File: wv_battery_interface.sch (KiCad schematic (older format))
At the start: 5 parts, among them J1 Conn_01x03, J11 Conn_01x03, J2 Conn_01x03, J3 Conn_01x04, U1 ATtiny204-SS

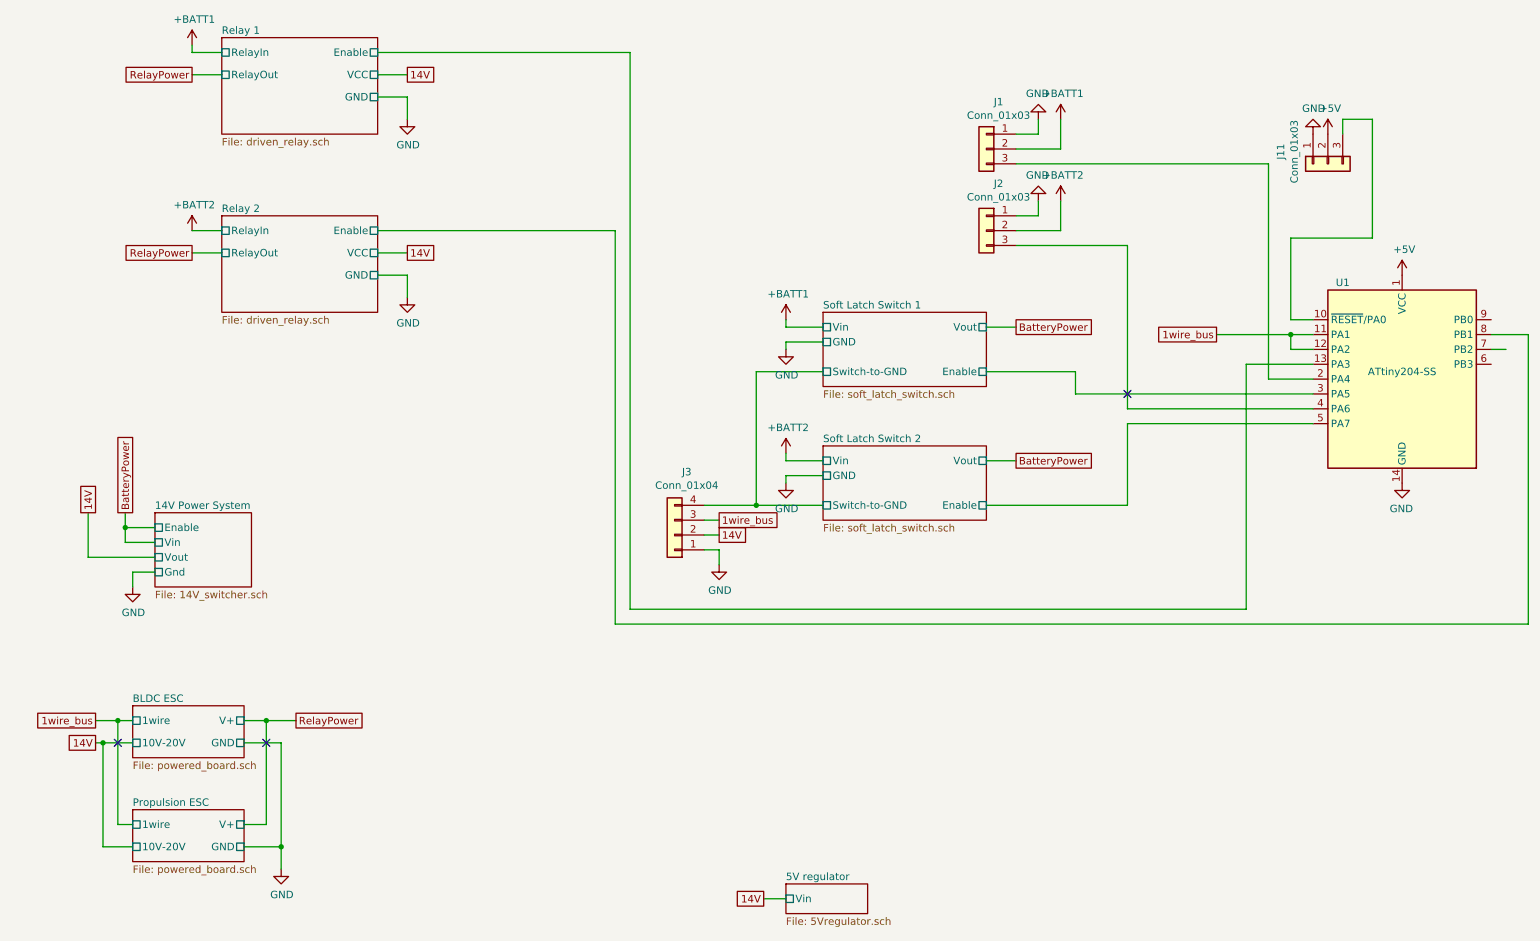
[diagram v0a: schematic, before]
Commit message: schematic update
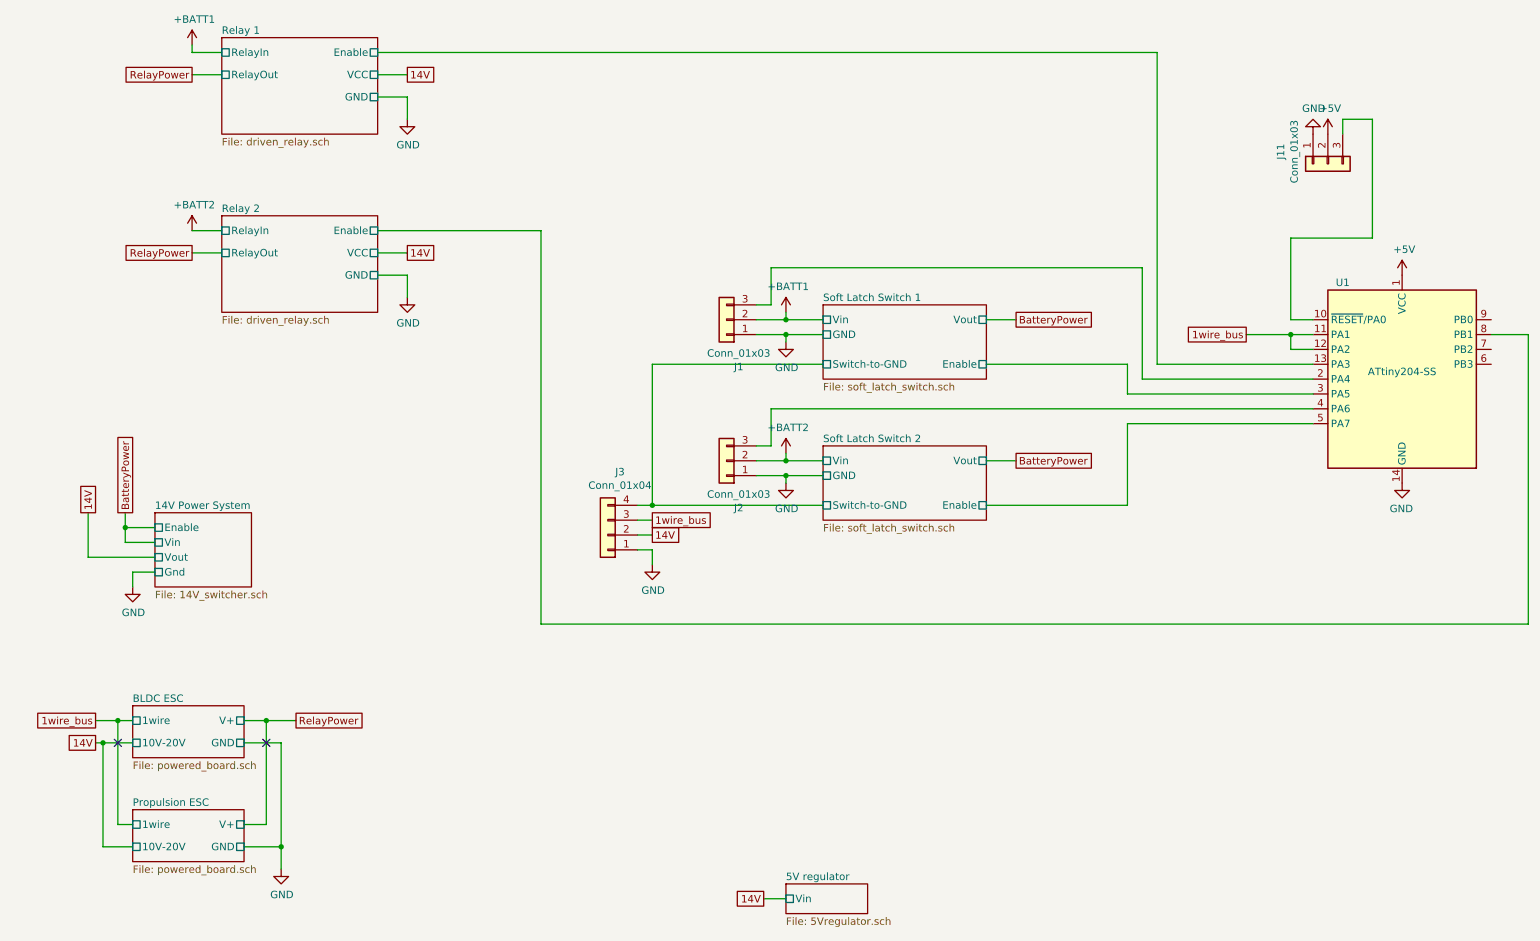
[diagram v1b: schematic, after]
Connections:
- no-connect marks 3 -> 2
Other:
- moved on the sheet: J1, J2, J3
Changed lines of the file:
@@
 $EndDescr
-$Comp
-L Connector_Generic:Conn_01x03 J1
-U 1 1 616238A4
-P 7250 2000
-F 0 "J1" H 7168 2317 50  0000 C CNN
-F 1 "Conn_01x03" H 7168 2226 50  0000 C CNN
-F 2 "Connector_Wire:SolderWire-2sqmm_1x03_P7.8mm_D2mm_OD3.9mm" H 7250 2000 50  0001 C CNN
-F 3 "~" H 7250 2000 50  0001 C CNN
-	1    7250 2000
-	-1   0    0    -1
-$EndComp
-$Comp
-L Connector_Generic:Conn_01x03 J2
-U 1 1 61623D8A
-P 7250 2550
-F 0 "J2" H 7168 2867 50  0000 C CNN
-F 1 "Conn_01x03" H 7168 2776 50  0000 C CNN
-F 2 "Connector_Wire:SolderWire-2sqmm_1x03_P7.8mm_D2mm_OD3.9mm" H 7250 2550 50  0001 C CNN
-F 3 "~" H 7250 2550 50  0001 C CNN
-	1    7250 2550
-	-1   0    0    -1
-$EndComp
-Wire Wire Line
-	7600 1900 7600 1800
-Wire Wire Line
-	7750 2000 7750 1800
-Wire Wire Line
-	7450 2450 7600 2450
-Wire Wire Line
-	7600 2450 7600 2350
-Wire Wire Line
-	7450 2550 7750 2550
-Wire Wire Line
-	7750 2550 7750 2350
-$Comp
-L power_symbols:+BATT1 #PWR0101
-U 1 1 61636C34
-P 7750 1800
-F 0 "#PWR0101" H 7750 1650 50  0001 C CNN
-F 1 "+BATT1" H 7765 1973 50  0000 C CNN
-F 2 "" H 7750 1800 50  0001 C CNN
-F 3 "" H 7750 1800 50  0001 C CNN
-	1    7750 1800
-	1    0    0    -1
-$EndComp
-Wire Wire Line
-	7450 2000 7750 2000
-Wire Wire Line
-	7450 1900 7600 1900
 $Comp
 L power_symbols:+BATT1 #PWR0106
@@
 L power_symbols:+BATT1 #PWR0107
 U 1 1 6168E4A3
-P 5900 3150
-F 0 "#PWR0107" H 5900 3000 50  0001 C CNN
-F 1 "+BATT1" H 5915 3323 50  0000 C CNN
-F 2 "" H 5900 3150 50  0001 C CNN
-F 3 "" H 5900 3150 50  0001 C CNN
-	1    5900 3150
-	1    0    0    -1
-$EndComp
-$Comp
-L power_symbols:+BATT2 #PWR0103
-U 1 1 61637B76
-P 7750 2350
-F 0 "#PWR0103" H 7750 2200 50  0001 C CNN
-F 1 "+BATT2" H 7765 2523 50  0000 C CNN
-F 2 "" H 7750 2350 50  0001 C CNN
-F 3 "" H 7750 2350 50  0001 C CNN
-	1    7750 2350
+P 5900 3100
+F 0 "#PWR0107" H 5900 2950 50  0001 C CNN
+F 1 "+BATT1" H 5915 3273 50  0000 C CNN
+F 2 "" H 5900 3100 50  0001 C CNN
+F 3 "" H 5900 3100 50  0001 C CNN
+	1    5900 3100
 	1    0    0    -1
 $EndComp
@@
 	1    0    0    -1
 $EndComp
-$Sheet
-S 6150 3100 1100 500
-U 6173FDB3
-F0 "Soft Latch Switch 1" 50
-F1 "soft_latch_switch.sch" 50
-F2 "Vin" U L 6150 3200 50
-F3 "GND" U L 6150 3300 50
-F4 "Vout" U R 7250 3200 50
-F5 "Enable" U R 7250 3500 50
-F6 "Switch-to-GND" U L 6150 3500 50
-$EndSheet
 $Sheet
 S 6150 4000 1100 500
@@
 	6150 4200 5900 4200
 Wire Wire Line
-	6150 3200 5900 3200
-Wire Wire Line
-	5900 3200 5900 3150
+	5900 3150 5900 3100
 $Comp
 L MCU_Microchip_ATtiny:ATtiny204-SS U1
@@
 L power:GND #PWR0114
 U 1 1 6179206F
-P 5450 4800
-F 0 "#PWR0114" H 5450 4550 50  0001 C CNN
-F 1 "GND" H 5455 4627 50  0000 C CNN
-F 2 "" H 5450 4800 50  0001 C CNN
-F 3 "" H 5450 4800 50  0001 C CNN
-	1    5450 4800
+P 5000 4800
+F 0 "#PWR0114" H 5000 4550 50  0001 C CNN
+F 1 "GND" H 5005 4627 50  0000 C CNN
+F 2 "" H 5000 4800 50  0001 C CNN
+F 3 "" H 5000 4800 50  0001 C CNN
+	1    5000 4800
 	1    0    0    -1
 $EndComp
@@
 	1400 5850 1500 5850
 Wire Wire Line
-	9450 3250 9300 3250
-Wire Wire Line
 	9300 3250 9300 3350
 Wire Wire Line
 	9300 3350 9450 3350
-Wire Wire Line
-	9300 3250 8800 3250
-Connection ~ 9300 3250
 $Sheet
 S 1650 4450 650  500
@@
 Wire Wire Line
 	1200 4450 1200 4750
-Text GLabel 8800 3250 0    50   UnSpc ~ 0
+Text GLabel 9000 3250 0    50   UnSpc ~ 0
 1wire_bus
 Text GLabel 1250 5850 0    50   UnSpc ~ 0
@@
 	1400 5850 1250 5850
 Connection ~ 1400 5850
-Text GLabel 5450 4500 2    50   UnSpc ~ 0
+Text GLabel 5000 4500 2    50   UnSpc ~ 0
 1wire_bus
 Text GLabel 1200 4450 1    50   UnSpc ~ 0
@@
 	2500 6850 2500 6700
 Connection ~ 2500 6700
-Text GLabel 7450 3200 2    50   UnSpc ~ 0
-BatteryPower
 Text GLabel 7450 4100 2    50   UnSpc ~ 0
 BatteryPower
@@
 L power:GND #PWR0112
 U 1 1 618C781F
-P 5900 3350
-F 0 "#PWR0112" H 5900 3100 50  0001 C CNN
-F 1 "GND" H 5905 3177 50  0000 C CNN
-F 2 "" H 5900 3350 50  0001 C CNN
-F 3 "" H 5900 3350 50  0001 C CNN
-	1    5900 3350
-	1    0    0    -1
-$EndComp
-Wire Wire Line
-	6150 3300 5900 3300
-Wire Wire Line
-	5900 3300 5900 3350
+P 5900 3300
+F 0 "#PWR0112" H 5900 3050 50  0001 C CNN
+F 1 "GND" H 5905 3127 50  0000 C CNN
+F 2 "" H 5900 3300 50  0001 C CNN
+F 3 "" H 5900 3300 50  0001 C CNN
+	1    5900 3300
+	1    0    0    -1
+$EndComp
+Wire Wire Line
+	5900 3250 5900 3300
 Text GLabel 1900 1500 0    50   UnSpc ~ 0
 RelayPower
@@
 L Connector_Generic:Conn_01x04 J3
 U 1 1 6178B2FF
-P 5150 4600
-F 0 "J3" H 5068 4175 50  0000 C CNN
-F 1 "Conn_01x04" H 5068 4266 50  0000 C CNN
-F 2 "Connector_PinHeader_2.54mm:PinHeader_1x04_P2.54mm_Vertical" H 5150 4600 50  0001 C CNN
-F 3 "~" H 5150 4600 50  0001 C CNN
-	1    5150 4600
+P 4700 4600
+F 0 "J3" H 4618 4175 50  0000 C CNN
+F 1 "Conn_01x04" H 4618 4266 50  0000 C CNN
+F 2 "Connector_PinHeader_2.54mm:PinHeader_1x04_P2.54mm_Vertical" H 4700 4600 50  0001 C CNN
+F 3 "~" H 4700 4600 50  0001 C CNN
+	1    4700 4600
 	-1   0    0    1
 $EndComp
-Text GLabel 5450 4600 2    50   UnSpc ~ 0
+Text GLabel 5000 4600 2    50   UnSpc ~ 0
 14V
 Wire Wire Line
-	5350 4700 5450 4700
-Wire Wire Line
-	5350 4600 5450 4600
-Wire Wire Line
-	5450 4500 5350 4500
-Wire Wire Line
-	5450 4700 5450 4800
+	4900 4700 5000 4700
+Wire Wire Line
+	4900 4600 5000 4600
+Wire Wire Line
+	5000 4500 4900 4500
+Wire Wire Line
+	5000 4700 5000 4800
 $Comp
 L power_symbols:+BATT2 #PWR0105
@@
 $EndComp
 Wire Wire Line
-	6150 3500 5700 3500
-Wire Wire Line
-	5700 3500 5700 4400
-Wire Wire Line
-	5700 4400 6150 4400
-Wire Wire Line
-	5350 4400 5700 4400
-Connection ~ 5700 4400
-Wire Wire Line
 	2400 5850 2400 6550
 Wire Wire Line
@@
 Wire Wire Line
 	1400 5850 1400 6550
-$Comp
-L power:GND #PWR0102
-U 1 1 6192AFDF
-P 7600 1800
-F 0 "#PWR0102" H 7600 1550 50  0001 C CNN
-F 1 "GND" H 7605 1627 50  0000 C CNN
-F 2 "" H 7600 1800 50  0001 C CNN
-F 3 "" H 7600 1800 50  0001 C CNN
-	1    7600 1800
-	-1   0    0    1
-$EndComp
-$Comp
-L power:GND #PWR0104
-U 1 1 6192BB15
-P 7600 2350
-F 0 "#PWR0104" H 7600 2100 50  0001 C CNN
-F 1 "GND" H 7605 2177 50  0000 C CNN
-F 2 "" H 7600 2350 50  0001 C CNN
-F 3 "" H 7600 2350 50  0001 C CNN
-	1    7600 2350
-	-1   0    0    1
-$EndComp
-Wire Wire Line
-	7450 2100 9150 2100
-Wire Wire Line
-	8200 2650 7450 2650
 $Sheet
 S 2100 1250 1050 650
@@
 Wire Wire Line
 	3150 2700 3350 2700
-Wire Wire Line
-	4850 5100 4850 1350
-Wire Wire Line
-	3150 1350 4850 1350
 Text GLabel 1450 4450 1    50   UnSpc ~ 0
 BatteryPower
 Wire Wire Line
-	4850 5100 9000 5100
-Wire Wire Line
 	10650 3250 10900 3250
 Wire Wire Line
-	3150 2550 4750 2550
-Wire Wire Line
-	4750 2550 4750 5200
-Wire Wire Line
-	4750 5200 10900 5200
+	3150 2550 4250 2550
 Wire Wire Line
 	10900 3250 10900 5200
-Wire Wire Line
-	9450 3450 9000 3450
-Wire Wire Line
-	9000 3450 9000 5100
-Wire Wire Line
-	10650 3350 10750 3350
-Wire Wire Line
-	9450 3650 7850 3650
-Wire Wire Line
-	7850 3650 7850 3500
-Wire Wire Line
-	9450 3550 9150 3550
-Wire Wire Line
-	9150 3550 9150 2100
-Wire Wire Line
-	9450 3750 8200 3750
-Wire Wire Line
-	8200 3750 8200 2650
 Wire Wire Line
 	9450 3850 8200 3850
@@
 	7250 4400 8200 4400
 Wire Wire Line
-	7250 3200 7450 3200
-Wire Wire Line
-	7250 3500 7850 3500
-NoConn ~ 8200 3650
+	8300 3550 8300 2800
+Wire Wire Line
+	8300 3550 9450 3550
+Wire Wire Line
+	8400 1350 8400 3450
+Wire Wire Line
+	3150 1350 8400 1350
+Wire Wire Line
+	8400 3450 9450 3450
+Wire Wire Line
+	9300 3250 9450 3250
+Wire Wire Line
+	9300 3250 9000 3250
+Connection ~ 9300 3250
+$Comp
+L Connector_Generic:Conn_01x03 J1
+U 1 1 616238A4
+P 5500 3150
+F 0 "J1" H 5418 3467 50  0000 C CNN
+F 1 "Conn_01x03" H 5418 3376 50  0000 C CNN
+F 2 "Connector_Wire:SolderWire-2sqmm_1x03_P7.8mm_D2mm_OD3.9mm" H 5500 3150 50  0001 C CNN
+F 3 "~" H 5500 3150 50  0001 C CNN
+	1    5500 3150
+	-1   0    0    1
+$EndComp
+$Comp
+L Connector_Generic:Conn_01x03 J2
+U 1 1 61623D8A
+P 5500 4100
+F 0 "J2" H 5418 4417 50  0000 C CNN
+F 1 "Conn_01x03" H 5418 4326 50  0000 C CNN
+F 2 "Connector_Wire:SolderWire-2sqmm_1x03_P7.8mm_D2mm_OD3.9mm" H 5500 4100 50  0001 C CNN
+F 3 "~" H 5500 4100 50  0001 C CNN
+	1    5500 4100
+	-1   0    0    1
+$EndComp
+Wire Wire Line
+	7250 3150 7450 3150
+Wire Wire Line
+	6150 3250 5900 3250
+Text GLabel 7450 3150 2    50   UnSpc ~ 0
+BatteryPower
+Wire Wire Line
+	6150 3150 5900 3150
+$Sheet
+S 6150 3050 1100 500
+U 6173FDB3
+F0 "Soft Latch Switch 1" 50
+F1 "soft_latch_switch.sch" 50
+F2 "Vin" U L 6150 3150 50
+F3 "GND" U L 6150 3250 50
+F4 "Vout" U R 7250 3150 50
+F5 "Enable" U R 7250 3450 50
+F6 "Switch-to-GND" U L 6150 3450 50
+$EndSheet
+Wire Wire Line
+	7250 3450 8200 3450
+Wire Wire Line
+	8200 3650 9450 3650
+Wire Wire Line
+	5700 4000 5800 4000
+Wire Wire Line
+	5800 4000 5800 3750
+Wire Wire Line
+	5800 3750 9450 3750
+Wire Wire Line
+	5700 4100 5900 4100
+Connection ~ 5900 4100
+Wire Wire Line
+	5900 4200 5700 4200
+Connection ~ 5900 4200
+Wire Wire Line
+	4900 4400 5000 4400
+Wire Wire Line
+	5700 3150 5900 3150
+Connection ~ 5900 3150
+Wire Wire Line
+	5900 3250 5700 3250
+Connection ~ 5900 3250
+Wire Wire Line
+	5700 3050 5800 3050
+Wire Wire Line
+	5800 3050 5800 2800
+Wire Wire Line
+	5800 2800 8300 2800
+Wire Wire Line
+	8200 3450 8200 3650
+Wire Wire Line
+	5000 3450 5000 4400
+Wire Wire Line
+	5000 3450 6150 3450
+Connection ~ 5000 4400
+Wire Wire Line
+	5000 4400 6150 4400
+Wire Wire Line
+	4250 5200 4250 2550
+Wire Wire Line
+	4250 5200 10900 5200
 $EndSCHEMATC

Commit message: schematic cleanup
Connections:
- net 1wire_bus is gone; now on net 14V: J3.3 (Pin_3), U1.11 (PA1), U1.12 (PA2)
- no-connect marks 2 -> 3
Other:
- moved on the sheet: J1, J11, J2, J3, U1
